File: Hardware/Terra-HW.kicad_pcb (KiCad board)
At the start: 4 copper layers, 76.9 x 67.3 mm, 95 parts, among them J1 GT-USB-7010ASV, J2 S2B-PH-SM4-TB, J3 0532610271, J4 Conn_Coaxial, J5 B8B-PH-SM4-TB, Q1 DMP3099L, Q2 2N7002, SW2 KMR231NG, SW3 KMR231NG, SW4 KMR231NG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

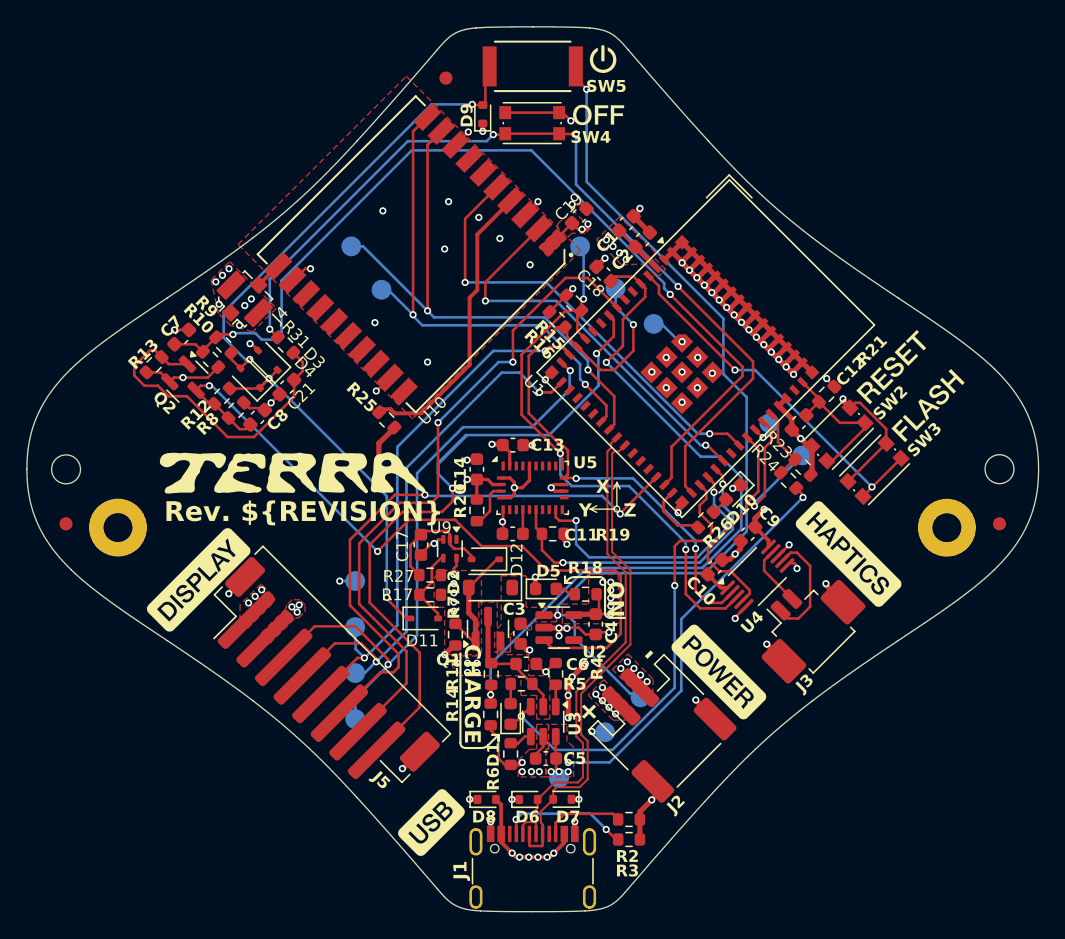
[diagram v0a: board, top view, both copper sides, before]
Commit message: more subtle silkscreen labeling per MODEM
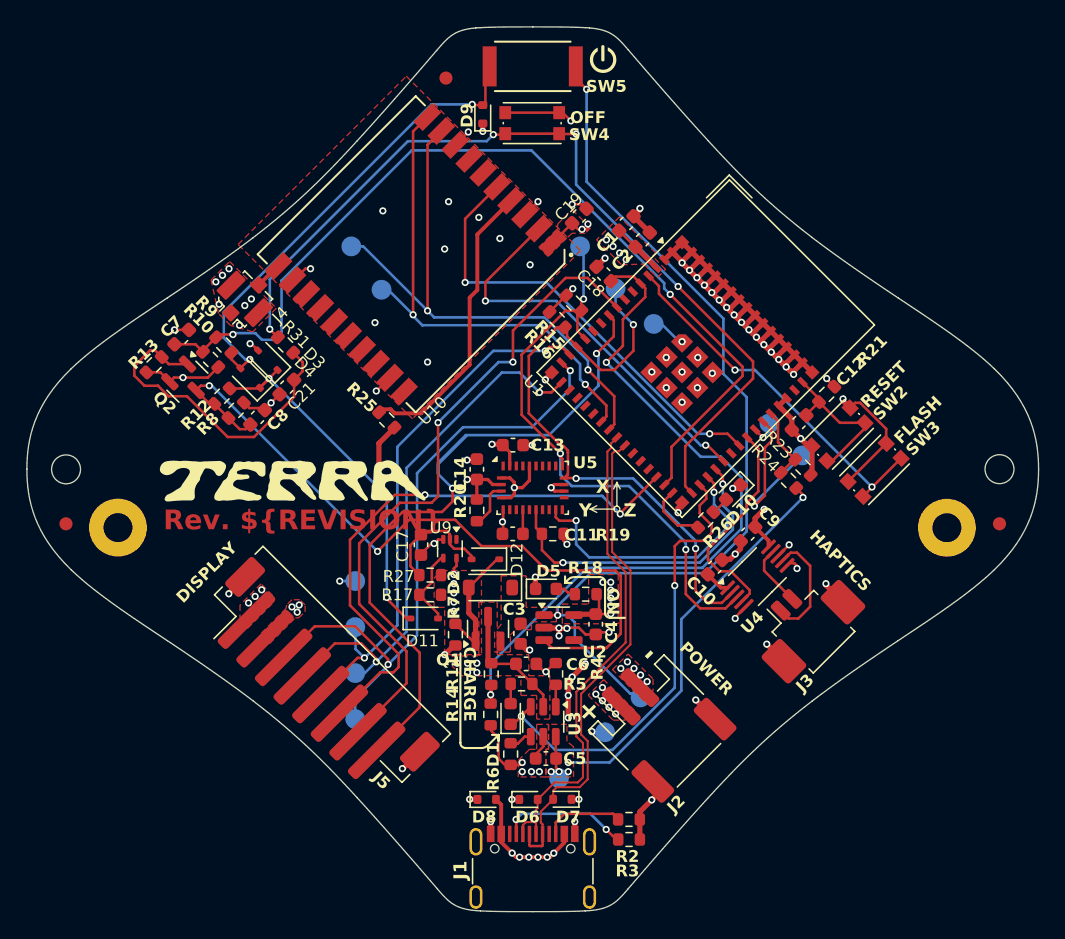
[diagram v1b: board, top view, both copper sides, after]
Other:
- board text added: "DISPLAY"
- board text added: "FLASH"
- board text added: "HAPTICS"
- board text added: "OFF"
- board text added: "POWER"
- board text added: "RESET"

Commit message: change D10 to white and move near power button
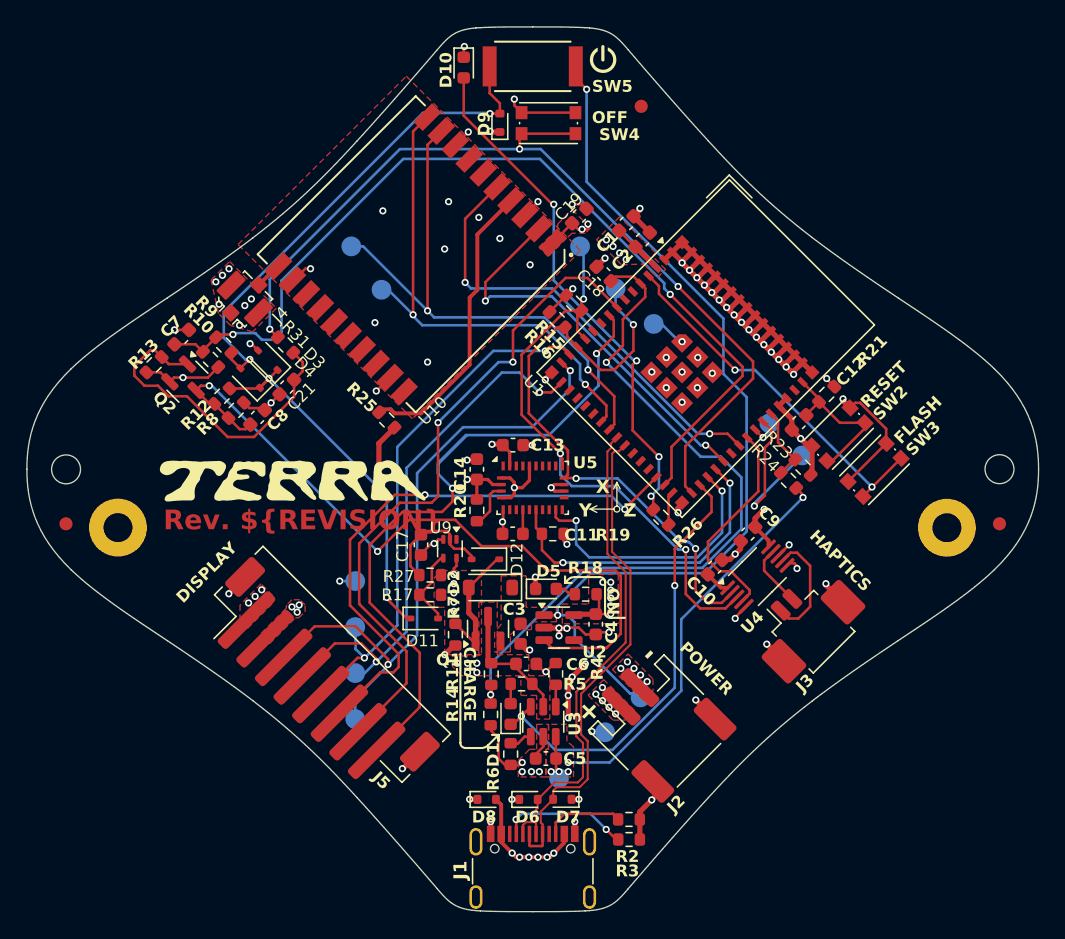
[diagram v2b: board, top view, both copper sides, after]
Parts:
- moved D10 38.3 mm to (144.8, 61.5), turned to -90 degrees
- moved FID2 15.0 mm to (158.3, 64.5)
- moved R26 3.41 mm to (159.8, 95.7), turned to 135 degrees
- moved D9 1.45 mm to (147.5, 65.7)
- moved SW4 1.24 mm to (151.2, 65.7)
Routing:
- net Net-(D10-A): track 1.41 -> 39.7 mm, vias 0 -> 4
- net Net-(D4-A): track 36.0 -> 39.2 mm
- net /Microcontroller/LED_GPIO48: track 4.94 -> 2.56 mm
- net /Microcontroller/PWROFF: track 67.8 -> 70.0 mm, vias 4 -> 3
- net /Microcontroller/BAT_~{CHG}: track 35.0 -> 33.5 mm
- net /Microcontroller/PWR_SW: track 71.0 -> 70.5 mm

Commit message: prepare export for Rev A
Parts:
- U10: value PA1616D -> ADAFRUIT PA1616D
- moved FID2 1.56 mm to (159.4, 65.5)
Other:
- board text added: "NOTE: DIODE POLARITY - CATHODE (-) MARKED WITH BAR/LINE ON SILKSCREEN LAYER -> |"
- board text removed: "ON"
